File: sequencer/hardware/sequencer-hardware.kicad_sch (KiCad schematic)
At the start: 48 parts

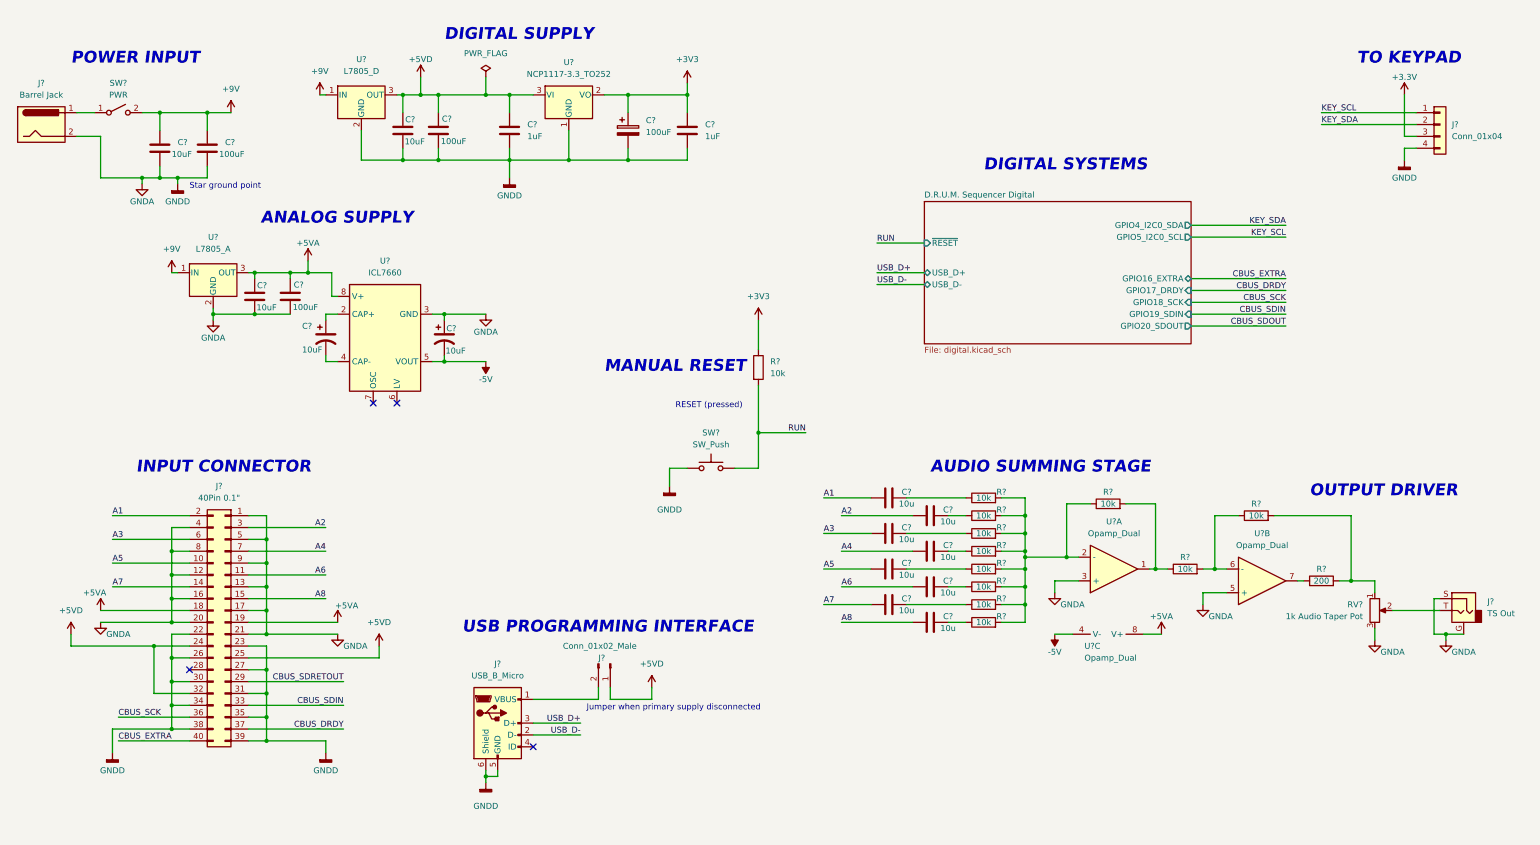
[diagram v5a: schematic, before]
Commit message: Fix scan chain pin labeling on input connector
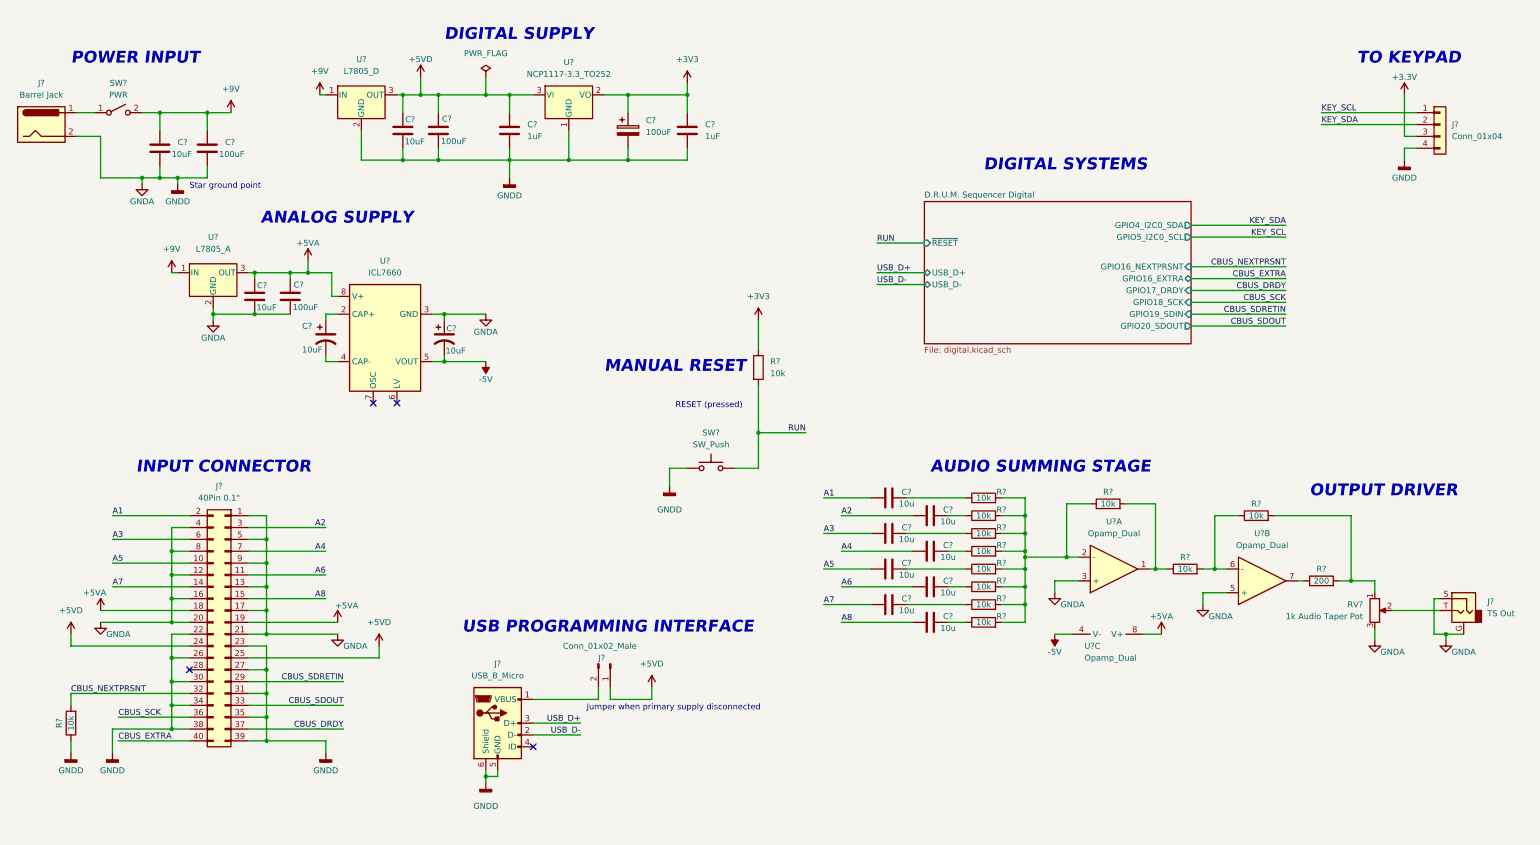
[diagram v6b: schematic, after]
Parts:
- added R?: 10k, symbol Device:R
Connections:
- net CBUS_SDIN is gone; now on net CBUS_SDOUT: J?.33 (Pin_33)
- net +5VD: no longer J?.32 (Pin_32)
- net GNDA: now also R?.1
- net CBUS_SDRETOUT renamed CBUS_SDRETIN
- new net CBUS_NEXTPRSNT: J?.32 (Pin_32), R?.2
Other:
- sheet D.R.U.M. Sequencer Digital ports: added GPIO16_NEXTPRSNT; removed none
- company: (none) -> D.R.U.M.
- title: (none) -> DRUM System Sequencer
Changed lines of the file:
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@@
 (kicad_sch (version 20211123) (generator eeschema)
   (paper "USLegal")
+  (title_block
+    (title "DRUM System Sequencer")
+    (date "2022-10-12")
+    (rev "1.0")
+    (company "D.R.U.M.")
+  )
   (junction (at 120.65 48.26) (diameter 0) (color 0 0 0 0)
   )
@@
   )
   (junction (at 231.14 133.35) (diameter 0) (color 0 0 0 0)
-  )
-  (junction (at 44.45 152.4) (diameter 0) (color 0 0 0 0)
   )
   (junction (at 48.26 160.02) (diameter 0) (color 0 0 0 0)
@@
     (stroke (width 0) (type default) (color 0 0 0 0))
   )
-  (wire (pts (xy 44.45 162.56) (xy 44.45 152.4))
-    (stroke (width 0) (type default) (color 0 0 0 0))
-  )
   (wire (pts (xy 83.82 81.28) (xy 81.28 81.28))
     (stroke (width 0) (type default) (color 0 0 0 0))
@@
     (stroke (width 0) (type default) (color 0 0 0 0))
   )
-  (wire (pts (xy 52.07 162.56) (xy 44.45 162.56))
+  (wire (pts (xy 26.67 162.56) (xy 52.07 162.56))
     (stroke (width 0) (type default) (color 0 0 0 0))
   )
@@
     (stroke (width 0) (type default) (color 0 0 0 0))
   )
+  (wire (pts (xy 266.7 71.12) (xy 287.02 71.12))
+    (stroke (width 0) (type default) (color 0 0 0 0))
+  )
   (wire (pts (xy 49.53 53.34) (xy 49.53 52.07))
     (stroke (width 0) (type default) (color 0 0 0 0))
@@
     (stroke (width 0) (type default) (color 0 0 0 0))
   )
-  (wire (pts (xy 26.67 152.4) (xy 44.45 152.4))
-    (stroke (width 0) (type default) (color 0 0 0 0))
-  )
   (wire (pts (xy 97.79 48.26) (xy 105.41 48.26))
     (stroke (width 0) (type default) (color 0 0 0 0))
@@
     (stroke (width 0) (type default) (color 0 0 0 0))
   )
+  (wire (pts (xy 26.67 165.1) (xy 26.67 162.56))
+    (stroke (width 0) (type default) (color 0 0 0 0))
+  )
   (wire (pts (xy 187.96 128.27) (xy 198.12 128.27))
     (stroke (width 0) (type default) (color 0 0 0 0))
@@
     (stroke (width 0) (type default) (color 0 0 0 0))
   )
-  (wire (pts (xy 44.45 152.4) (xy 52.07 152.4))
+  (wire (pts (xy 26.67 152.4) (xy 52.07 152.4))
     (stroke (width 0) (type default) (color 0 0 0 0))
   )
@@
   )
   (wire (pts (xy 142.24 161.29) (xy 142.24 163.83))
+    (stroke (width 0) (type default) (color 0 0 0 0))
+  )
+  (wire (pts (xy 26.67 172.72) (xy 26.67 175.26))
     (stroke (width 0) (type default) (color 0 0 0 0))
   )
@@
     (effects (font (size 1.27 1.27)) (justify left bottom))
   )
+  (label "CBUS_NEXTPRSNT" (at 287.02 71.12 180)
+    (effects (font (size 1.27 1.27)) (justify right bottom))
+  )
   (label "A8" (at 191.77 147.32 0)
     (effects (font (size 1.27 1.27)) (justify left bottom))
@@
     (effects (font (size 1.27 1.27)) (justify left bottom))
   )
-  (label "CBUS_SDIN" (at 287.02 81.28 180)
+  (label "CBUS_SDRETIN" (at 287.02 81.28 180)
     (effects (font (size 1.27 1.27)) (justify right bottom))
   )
@@
     (effects (font (size 1.27 1.27)) (justify right bottom))
   )
+  (label "CBUS_NEXTPRSNT" (at 26.67 162.56 0)
+    (effects (font (size 1.27 1.27)) (justify left bottom))
+  )
   (label "A3" (at 187.96 128.27 0)
     (effects (font (size 1.27 1.27)) (justify left bottom))
@@
     (effects (font (size 1.27 1.27)) (justify right bottom))
   )
-  (label "CBUS_SDRETOUT" (at 85.09 160.02 180)
+  (label "CBUS_SDRETIN" (at 85.09 160.02 180)
     (effects (font (size 1.27 1.27)) (justify right bottom))
   )
@@
     (effects (font (size 1.27 1.27)) (justify right bottom))
   )
-  (label "CBUS_SDIN" (at 85.09 165.1 180)
+  (label "CBUS_SDOUT" (at 85.09 165.1 180)
     (effects (font (size 1.27 1.27)) (justify right bottom))
   )
@@
     )
     (property "Datasheet" "~" (id 3) (at 163.83 109.22 0)
+      (effects (font (size 1.27 1.27)) hide)
+    )
+    (pin "1")
+    (pin "2")
+  )
+  (symbol (lib_id "Device:R") (at 26.67 168.91 180) (unit 1)
+    (in_bom yes) (on_board yes)
+    (property "Reference" "R?" (id 0) (at 24.13 168.91 90))
+    (property "Value" "10k" (id 1) (at 26.67 168.91 90))
+    (property "Footprint" "" (id 2) (at 28.448 168.91 90)
+      (effects (font (size 1.27 1.27)) hide)
+    )
+    (property "Datasheet" "~" (id 3) (at 26.67 168.91 0)
       (effects (font (size 1.27 1.27)) hide)
     )
@@
     (pin "1")
   )
+  (symbol (lib_id "power:GNDD") (at 26.67 175.26 0) (unit 1)
+    (in_bom yes) (on_board yes)
+    (property "Reference" "#PWR?" (id 0) (at 26.67 181.61 0)
+      (effects (font (size 1.27 1.27)) hide)
+    )
+    (property "Value" "GNDD" (id 1) (at 26.67 179.07 0))
+    (property "Footprint" "" (id 2) (at 26.67 175.26 0)
+      (effects (font (size 1.27 1.27)) hide)
+    )
+    (property "Datasheet" "" (id 3) (at 26.67 175.26 0)
+      (effects (font (size 1.27 1.27)) hide)
+    )
+    (pin "1")
+  )
   (symbol (lib_id "power:GNDA") (at 306.07 151.13 0) (mirror y) (unit 1)
     (in_bom yes) (on_board yes)
@@
       (effects (font (size 1.27 1.27)) (justify right))
     )
+    (pin "GPIO16_NEXTPRSNT" input (at 266.7 71.12 0)
+      (effects (font (size 1.27 1.27)) (justify right))
+    )
   )
   (sheet_instances
@@
       (reference "#PWR?") (unit 1) (value "+5VA") (footprint "")
     )
+    (path "/f90854a7-1815-4b3e-9b6f-92cfc769a37b"
+      (reference "#PWR?") (unit 1) (value "GNDD") (footprint "")
+    )
     (path "/fc637bc4-4334-497c-8fc0-3b424642545e"
       (reference "#PWR?") (unit 1) (value "GNDA") (footprint "")
@@
       (reference "R?") (unit 1) (value "10k") (footprint "Resistor_SMD:R_0603_1608Metric_Pad0.98x0.95mm_HandSolder")
     )
+    (path "/d1178891-9012-4ece-af80-f2acf0ed95f0"
+      (reference "R?") (unit 1) (value "10k") (footprint "")
+    )
     (path "/56dcffd5-e973-4f89-956d-68b94266f270/ea3847a1-dcc8-45de-85bf-3485ae8a8824"

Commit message: Add optional pulldown resistors to buttons
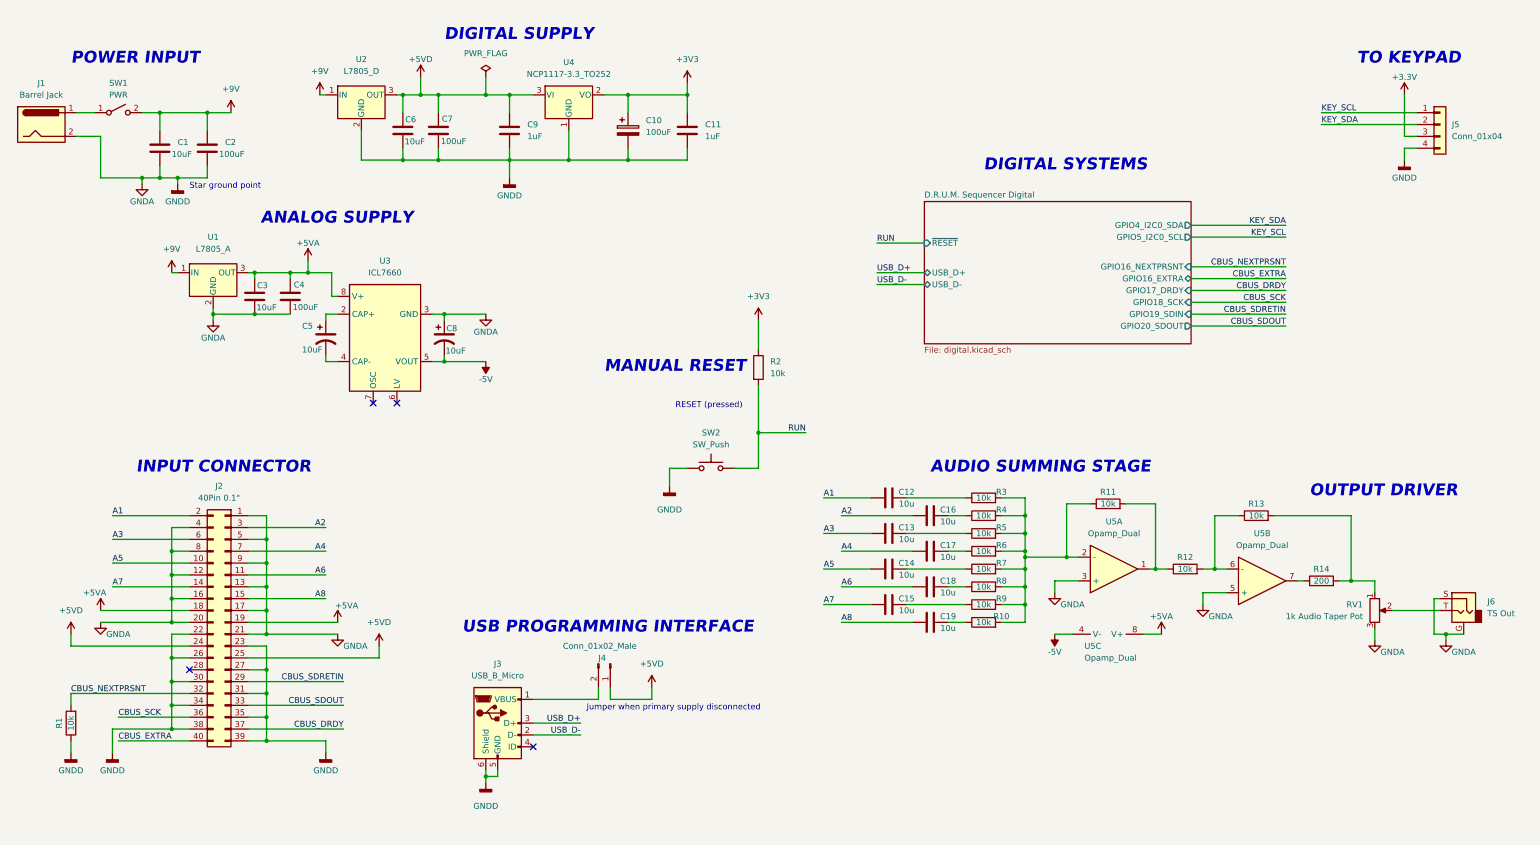
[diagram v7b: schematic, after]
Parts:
- C12, C13, C14, C15, C16, C17, C18, C19: renamed from C?; footprint (none) -> Capacitor_SMD:C_1206_3216Metric_Pad1.33x1.80mm_HandSolder
- J2: renamed from J?; footprint (none) -> Connector_PinHeader_2.54mm:PinHeader_2x20_P2.54mm_Horizontal
- gave numbers to parts that had none: 38
